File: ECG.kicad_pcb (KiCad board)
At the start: 2 copper layers, 40.6 x 23 mm, 32 parts, among them P1 RA, P2 LL, P3 RL, P4 OUT, P5 5V, P6 GND, P7 Shield, P8 Out_ina, U1 INA333, U2 OPA2335, U3 OPA2335, U4 REF5050, U5 REF3125

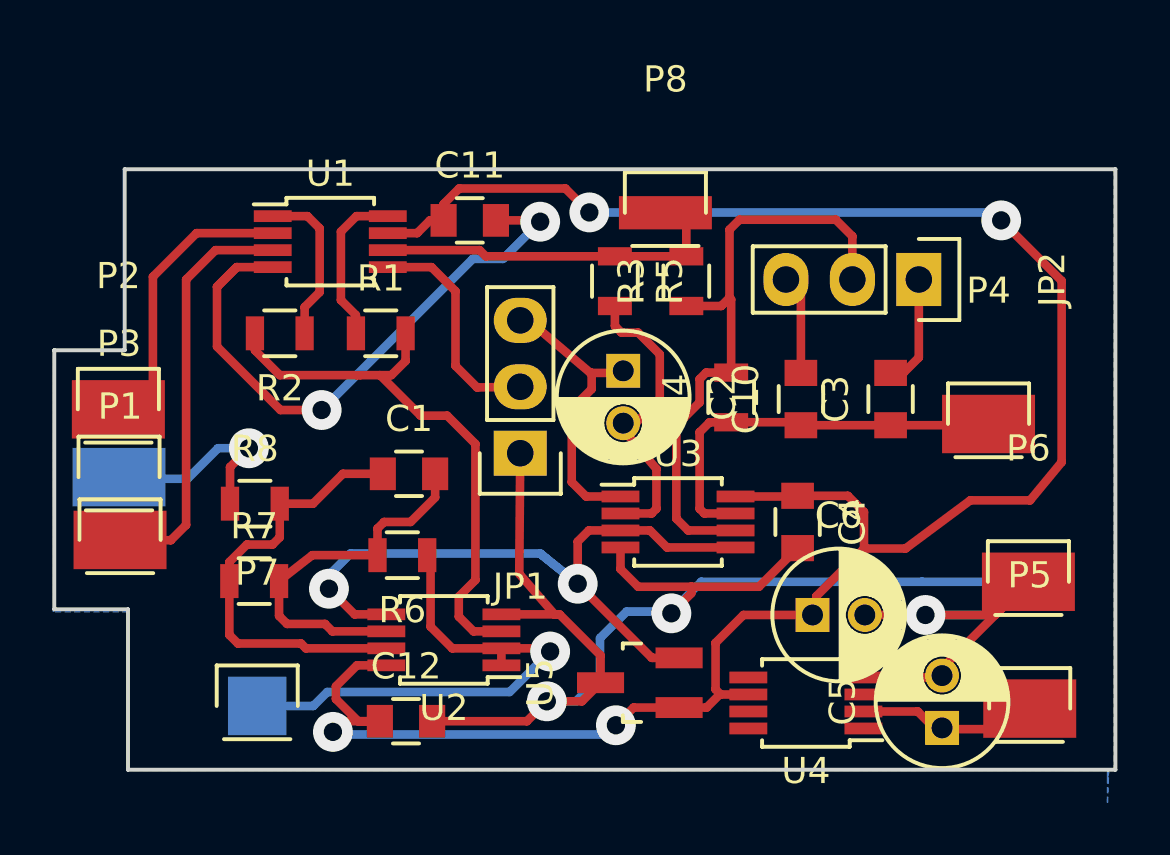
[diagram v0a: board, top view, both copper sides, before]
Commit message: PCB
Placa con nombre. Correcciones del plano y edge
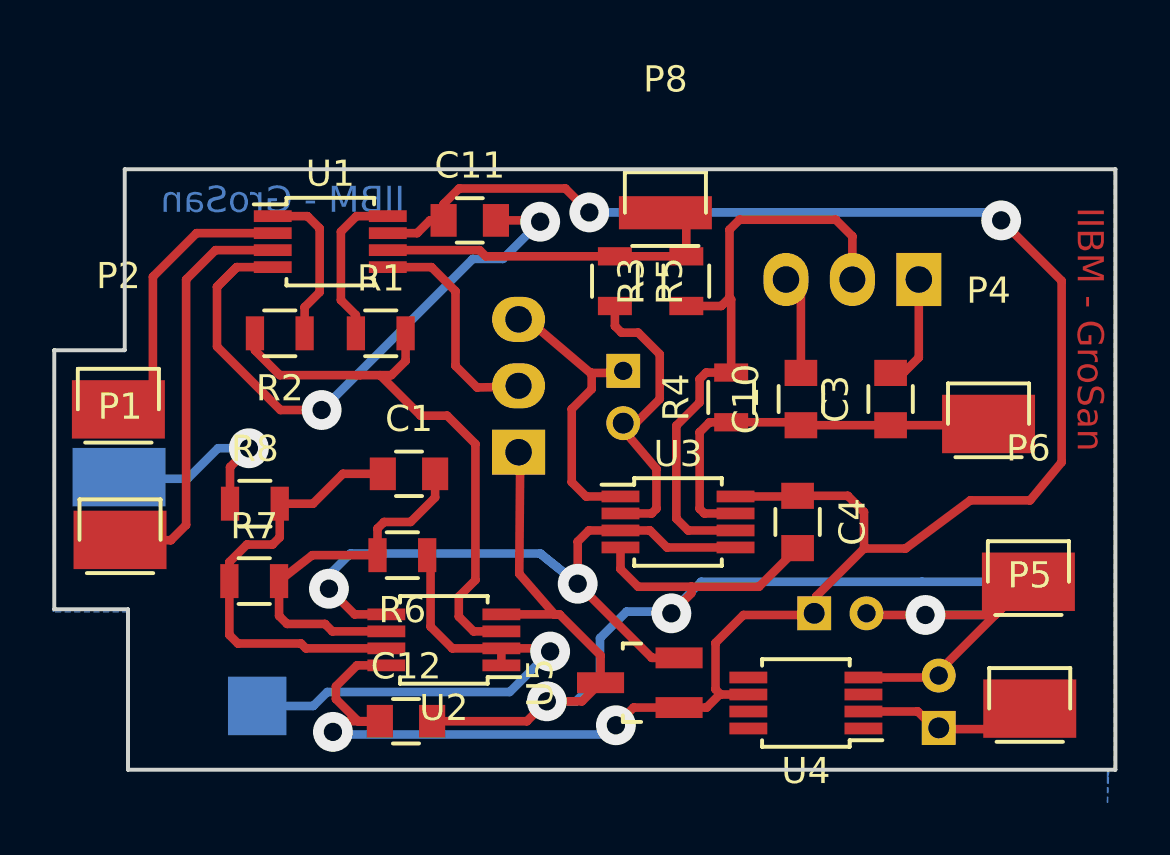
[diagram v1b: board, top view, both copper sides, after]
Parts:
- C2, C5, C6, JP1, JP2, P3, P7: moved to B.Cu
- moved C5 0.13 mm to (145.0, 88.9)
- moved C6 0.09 mm to (140.3, 84.5)
- moved JP1 0.07 mm to (129.0, 78.4), turned to 0 degrees
- turned JP2 to 90 degrees
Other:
- board text added: "IIBM - GroSan"
